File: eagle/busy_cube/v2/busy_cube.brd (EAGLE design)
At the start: 108 x 45.7 mm, 14 parts

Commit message: Cleaner version of v2
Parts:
- removed R2: 0, busy_cube_lib:1206
- moved U$1 7.62 mm to (35.6, 24.1)
- moved LIS3DH 6.35 mm to (35.6, 7.62)
- moved NEO_PIXELS 5.08 mm to (3.81, 21.6), turned to 90 degrees
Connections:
- removed net N$8: LIS3DH.SDA, R2.2
- net N$5: now also LIS3DH.SDA; no longer R2.1
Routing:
- net GND: track 182.9 -> 18.5 mm, vias 0 -> 6
- net N$9: track 0.00 -> 7.66 mm
- net SPKR: track 0.00 -> 7.40 mm
- net N$11: track 42.6 -> 36.1 mm
- net N$5: track 13.8 -> 8.15 mm
- net N$8: track 4.28 -> 0.00 mm
- net VCC: track 79.3 -> 82.7 mm
- net N$3: track 7.40 -> 5.08 mm
- net N$4: track 7.02 -> 5.61 mm
- net N$6: track 6.88 -> 5.61 mm
- net N$1: track 10.7 -> 9.42 mm
- net BTN1: track 14.5 -> 13.5 mm
- net N$2: track 5.39 -> 6.13 mm
- net NEO_RES: vias 0 -> 1
- added copper zone on layer 16, net GND
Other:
- board size 108 x 45.7 mm -> 108 x 43.2 mm
- board text removed: "View from bottom"

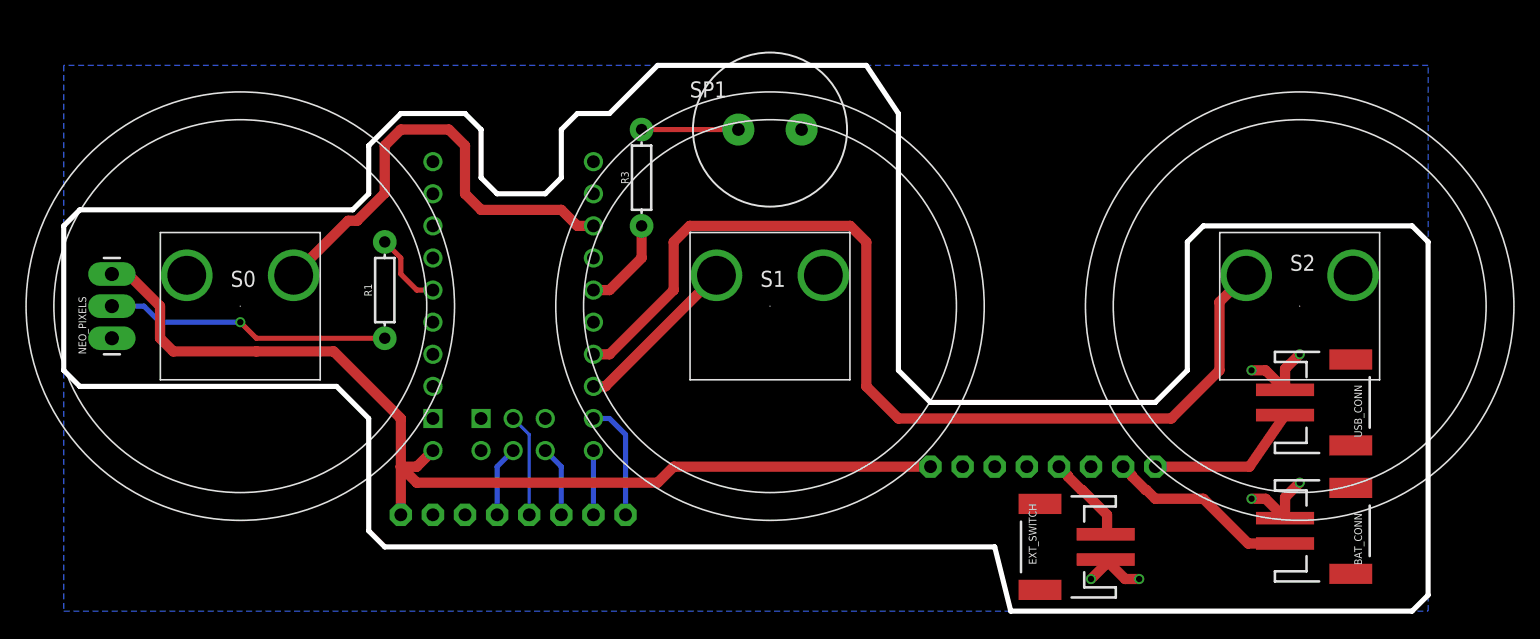
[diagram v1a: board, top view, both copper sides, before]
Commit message: Large pads and holes for the buttons
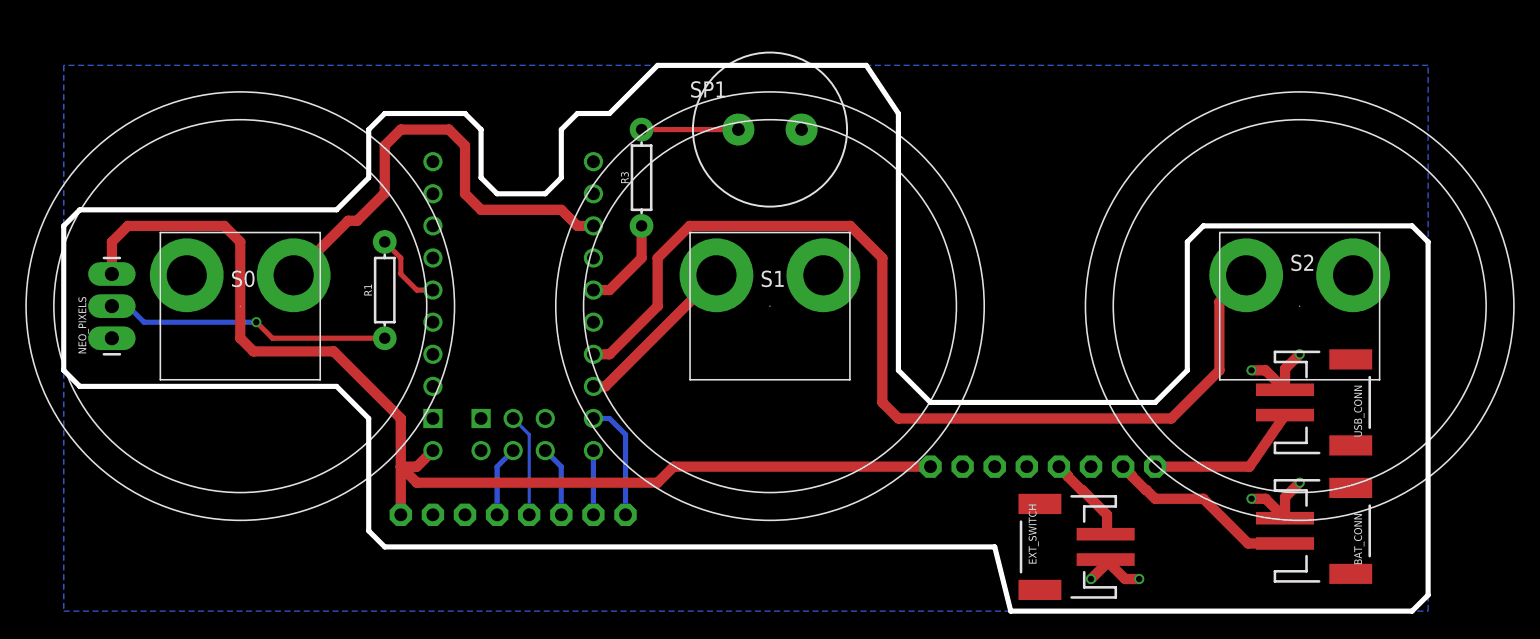
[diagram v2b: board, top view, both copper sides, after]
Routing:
- net VCC: track 82.7 -> 90.4 mm
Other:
- outline, holes or cut-outs redrawn
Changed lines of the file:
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@@
 <wire x1="66.04" y1="39.37" x2="63.5" y2="43.18" width="0.4064" layer="20"/>
 <wire x1="63.5" y1="43.18" x2="46.99" y2="43.18" width="0.4064" layer="20"/>
-<wire x1="26.67" y1="39.37" x2="24.13" y2="36.83" width="0.4064" layer="20"/>
+<wire x1="25.4" y1="39.37" x2="24.13" y2="38.1" width="0.4064" layer="20"/>
 <wire x1="1.27" y1="31.75" x2="0" y2="30.48" width="0.4064" layer="20"/>
 <wire x1="88.9" y1="19.05" x2="88.9" y2="29.21" width="0.4064" layer="20"/>
@@
 <wire x1="107.95" y1="1.27" x2="107.95" y2="29.21" width="0.4064" layer="20"/>
 <wire x1="106.68" y1="0" x2="107.95" y2="1.27" width="0.4064" layer="20"/>
-<wire x1="24.13" y1="36.83" x2="24.13" y2="33.02" width="0.4064" layer="20"/>
-<wire x1="24.13" y1="33.02" x2="22.86" y2="31.75" width="0.4064" layer="20"/>
-<wire x1="22.86" y1="31.75" x2="1.27" y2="31.75" width="0.4064" layer="20"/>
+<wire x1="24.13" y1="38.1" x2="24.13" y2="34.29" width="0.4064" layer="20"/>
+<wire x1="24.13" y1="34.29" x2="21.59" y2="31.75" width="0.4064" layer="20"/>
+<wire x1="21.59" y1="31.75" x2="1.27" y2="31.75" width="0.4064" layer="20"/>
 <wire x1="0" y1="30.48" x2="0" y2="19.05" width="0.4064" layer="20"/>
 <wire x1="0" y1="19.05" x2="1.27" y2="17.78" width="0.4064" layer="20"/>
@@
 <wire x1="73.66" y1="5.08" x2="74.93" y2="0" width="0.4064" layer="20"/>
 <wire x1="43.18" y1="39.37" x2="46.99" y2="43.18" width="0.4064" layer="20"/>
-<wire x1="26.67" y1="39.37" x2="31.75" y2="39.37" width="0.4064" layer="20"/>
+<wire x1="25.4" y1="39.37" x2="31.75" y2="39.37" width="0.4064" layer="20"/>
 <wire x1="31.75" y1="39.37" x2="33.02" y2="38.1" width="0.4064" layer="20"/>
 <wire x1="33.02" y1="38.1" x2="33.02" y2="34.29" width="0.4064" layer="20"/>
@@
 </class>
 </classes>
-<designrules name="ITEADstudio_DRC">
+<designrules name="PCBNG_DRC_by_oren">
 <description language="de">&lt;b&gt;EAGLE Design Rules&lt;/b&gt;
 &lt;p&gt;
@@
 <param name="mdViaViaSameLayer" value="8mil"/>
 <param name="mnLayersViaInSmd" value="2"/>
-<param name="mdCopperDimension" value="10mil"/>
-<param name="mdDrill" value="10mil"/>
+<param name="mdCopperDimension" value="20mil"/>
+<param name="mdDrill" value="20mil"/>
 <param name="mdSmdStop" value="0mil"/>
-<param name="msWidth" value="6mil"/>
+<param name="msWidth" value="4mil"/>
 <param name="msDrill" value="12mil"/>
-<param name="msMicroVia" value="12mil"/>
+<param name="msMicroVia" value="18mil"/>
 <param name="msBlindViaRatio" value="0.5"/>
 <param name="rvPadTop" value="0.25"/>
@@
 <param name="mvCreamFrame" value="0"/>
 <param name="mlMinStopFrame" value="2mil"/>
-<param name="mlMaxStopFrame" value="2mil"/>
+<param name="mlMaxStopFrame" value="4mil"/>
 <param name="mlMinCreamFrame" value="0mil"/>
 <param name="mlMaxCreamFrame" value="0mil"/>
@@
 <contactref element="LIS3DH" pad="VIN"/>
 <contactref element="NEO_PIXELS" pad="3"/>
-<wire x1="15.24" y1="20.5486" x2="21.3614" y2="20.5486" width="0.8128" layer="1"/>
 <wire x1="21.3614" y1="20.5486" x2="26.67" y2="15.24" width="0.8128" layer="1"/>
 <wire x1="26.67" y1="15.24" x2="26.67" y2="11.43" width="0.8128" layer="1"/>
@@
 <wire x1="46.99" y1="10.16" x2="27.94" y2="10.16" width="0.8128" layer="1"/>
 <wire x1="27.94" y1="10.16" x2="26.67" y2="11.43" width="0.8128" layer="1"/>
-<wire x1="8.6614" y1="20.5486" x2="7.62" y2="21.59" width="0.8128" layer="1"/>
-<wire x1="7.62" y1="24.13" x2="5.08" y2="26.67" width="0.8128" layer="1"/>
-<wire x1="5.08" y1="26.67" x2="3.81" y2="26.67" width="0.8128" layer="1"/>
-<wire x1="15.24" y1="20.5486" x2="8.6614" y2="20.5486" width="0.8128" layer="1"/>
-<wire x1="7.62" y1="21.59" x2="7.62" y2="24.13" width="0.8128" layer="1"/>
+<wire x1="21.3614" y1="20.5486" x2="15.0114" y2="20.5486" width="0.8128" layer="1"/>
+<wire x1="15.0114" y1="20.5486" x2="13.97" y2="21.59" width="0.8128" layer="1"/>
+<wire x1="13.97" y1="21.59" x2="13.97" y2="29.21" width="0.8128" layer="1"/>
+<wire x1="13.97" y1="29.21" x2="12.7" y2="30.48" width="0.8128" layer="1"/>
+<wire x1="12.7" y1="30.48" x2="5.08" y2="30.48" width="0.8128" layer="1"/>
+<wire x1="5.08" y1="30.48" x2="3.81" y2="29.21" width="0.8128" layer="1"/>
+<wire x1="3.81" y1="29.21" x2="3.81" y2="26.67" width="0.8128" layer="1"/>
 </signal>
 <signal name="BTN2">
 <contactref element="S2" pad="T"/>
-<wire x1="63.5" y1="29.21" x2="62.23" y2="30.48" width="0.8128" layer="1"/>
-<wire x1="63.5" y1="29.21" x2="63.5" y2="17.78" width="0.8128" layer="1"/>
-<wire x1="63.5" y1="17.78" x2="66.04" y2="15.24" width="0.8128" layer="1"/>
+<wire x1="64.77" y1="27.94" x2="62.23" y2="30.48" width="0.8128" layer="1"/>
+<wire x1="64.77" y1="27.94" x2="64.77" y2="16.51" width="0.8128" layer="1"/>
+<wire x1="64.77" y1="16.51" x2="66.04" y2="15.24" width="0.8128" layer="1"/>
 <wire x1="66.04" y1="15.24" x2="87.63" y2="15.24" width="0.8128" layer="1"/>
 <wire x1="87.63" y1="15.24" x2="91.44" y2="19.05" width="0.8128" layer="1"/>
@@
 <wire x1="91.44" y1="24.455715625" x2="93.555215625" y2="26.57093125" width="0.8128" layer="1"/>
 <wire x1="62.23" y1="30.48" x2="49.53" y2="30.48" width="0.8128" layer="1"/>
-<wire x1="49.53" y1="30.48" x2="48.26" y2="29.21" width="0.8128" layer="1"/>
+<wire x1="49.53" y1="30.48" x2="46.99" y2="27.94" width="0.8128" layer="1"/>
 <contactref element="U$1" pad="3"/>
-<wire x1="48.26" y1="29.21" x2="48.26" y2="25.4" width="0.8128" layer="1"/>
-<wire x1="48.26" y1="25.4" x2="43.18" y2="20.32" width="0.8128" layer="1"/>
+<wire x1="46.99" y1="27.94" x2="46.99" y2="24.13" width="0.8128" layer="1"/>
+<wire x1="46.99" y1="24.13" x2="43.18" y2="20.32" width="0.8128" layer="1"/>
 <wire x1="43.18" y1="20.32" x2="41.91" y2="20.32" width="0.8128" layer="1"/>
 </signal>
@@
 <contactref element="R1" pad="P$1"/>
 <contactref element="NEO_PIXELS" pad="2"/>
-<wire x1="25.4" y1="21.59" x2="15.24" y2="21.59" width="0.4064" layer="1"/>
-<wire x1="15.24" y1="21.59" x2="13.97" y2="22.86" width="0.4064" layer="1"/>
-<via x="13.97" y="22.86" extent="1-16" drill="0.5"/>
-<wire x1="13.97" y1="22.86" x2="7.62" y2="22.86" width="0.4064" layer="16"/>
-<wire x1="7.62" y1="22.86" x2="6.35" y2="24.13" width="0.4064" layer="16"/>
-<wire x1="6.35" y1="24.13" x2="3.81" y2="24.13" width="0.4064" layer="16"/>
+<wire x1="25.4" y1="21.59" x2="16.51" y2="21.59" width="0.4064" layer="1"/>
+<wire x1="16.51" y1="21.59" x2="15.24" y2="22.86" width="0.4064" layer="1"/>
+<via x="15.24" y="22.86" extent="1-16" drill="0.5"/>
+<wire x1="15.24" y1="22.86" x2="6.35" y2="22.86" width="0.4064" layer="16"/>
+<wire x1="6.35" y1="22.86" x2="5.08" y2="24.13" width="0.4064" layer="16"/>
+<wire x1="5.08" y1="24.13" x2="3.81" y2="24.13" width="0.4064" layer="16"/>
 </signal>
 <signal name="BTN1">
